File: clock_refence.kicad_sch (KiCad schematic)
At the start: 52 parts, among them J204 REFOUT_AUX_P, J205 REFOUT_AUX_N, J206 RFShield_TwoPieces, J207 REFOUT, J209 DNP, T202 TC2-1T+, U201 Si53301, U202 XC6204B33

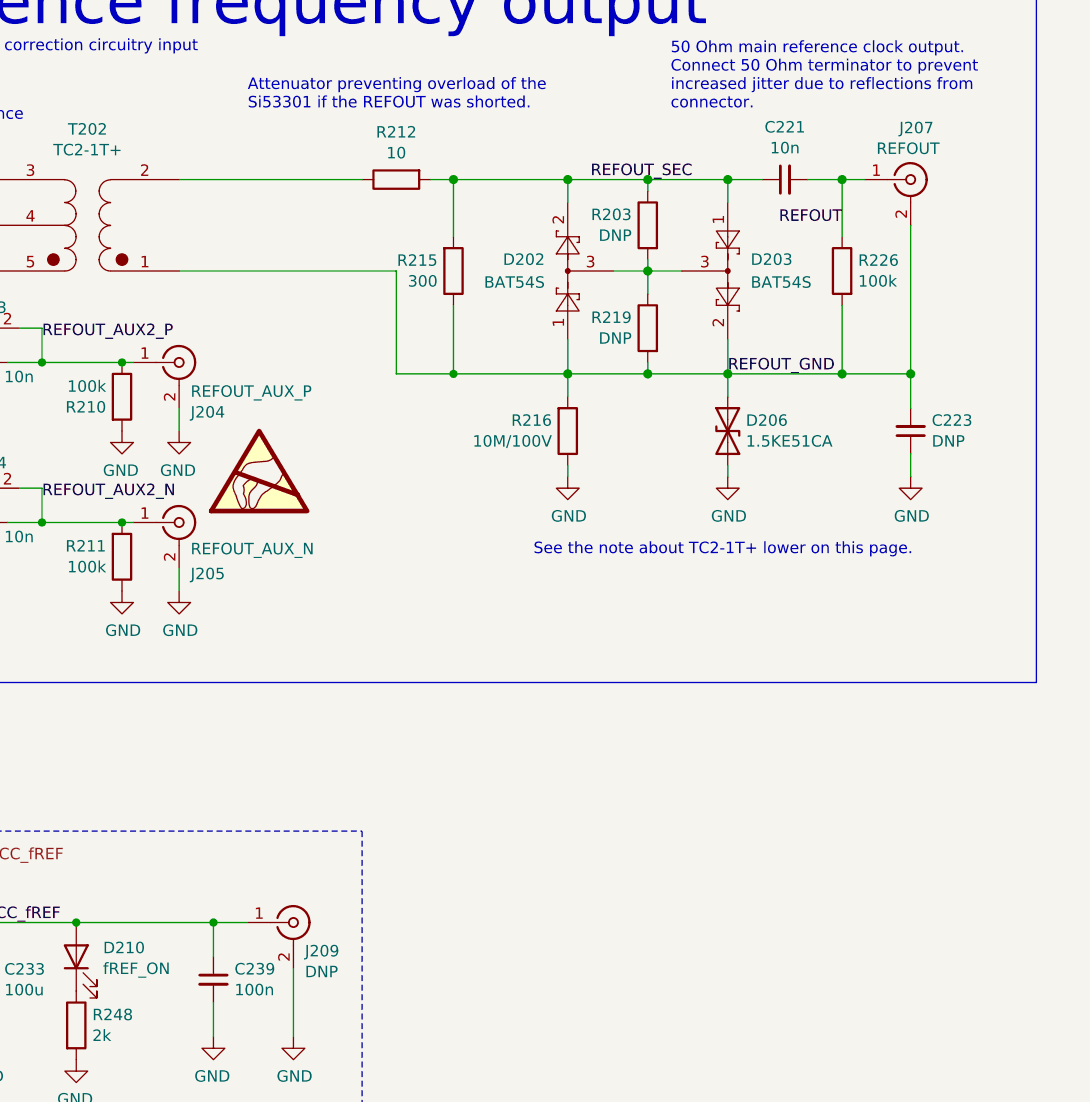
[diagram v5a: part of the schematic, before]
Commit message: Schematic fixes
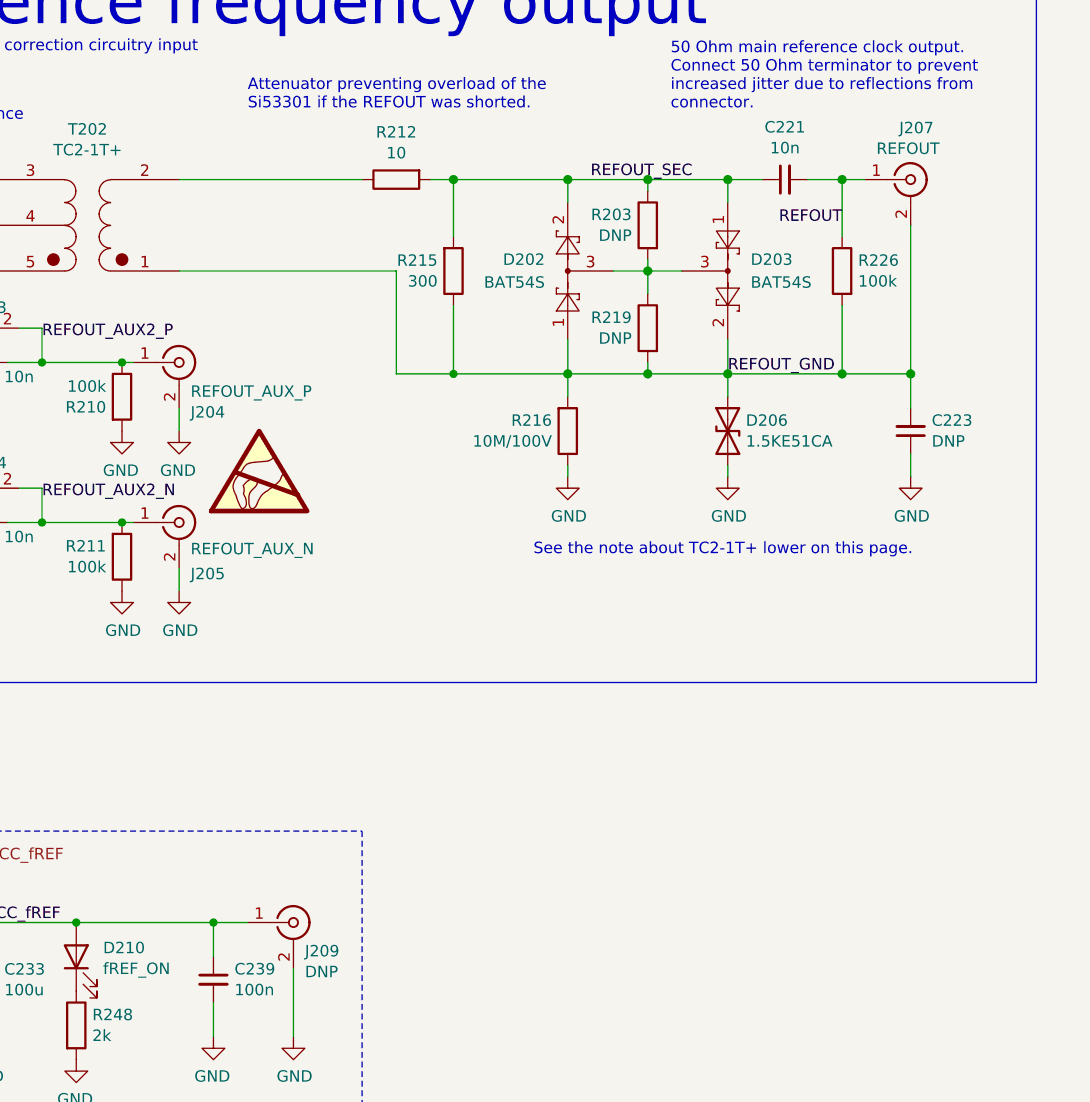
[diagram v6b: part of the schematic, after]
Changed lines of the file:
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@@
     (comment 3 "Dual channel symmetric outputs")
   )
+  (junction (at 111.76 175.26) (diameter 1.016) (color 0 0 0 0))
   (junction (at 29.21 175.26) (diameter 1.016) (color 0 0 0 0))
-  (junction (at 69.85 50.8) (diameter 1.016) (color 0 0 0 0))
+  (junction (at 118.11 130.81) (diameter 0.9144) (color 0 0 0 0))
+  (junction (at 127 130.81) (diameter 0.9144) (color 0 0 0 0))
+  (junction (at 55.88 50.8) (diameter 0.9144) (color 0 0 0 0))
+  (junction (at 127 113.03) (diameter 0.9144) (color 0 0 0 0))
+  (junction (at 207.01 92.71) (diameter 1.016) (color 0 0 0 0))
+  (junction (at 77.47 58.42) (diameter 0.9144) (color 0 0 0 0))
   (junction (at 85.09 50.8) (diameter 1.016) (color 0 0 0 0))
-  (junction (at 137.16 175.26) (diameter 0.9144) (color 0 0 0 0))
-  (junction (at 63.5 179.07) (diameter 1.016) (color 0 0 0 0))
+  (junction (at 185.42 102.87) (diameter 1.016) (color 0 0 0 0))
   (junction (at 64.77 50.8) (diameter 1.016) (color 0 0 0 0))
   (junction (at 185.42 92.71) (diameter 1.016) (color 0 0 0 0))
+  (junction (at 185.42 114.3) (diameter 1.016) (color 0 0 0 0))
+  (junction (at 163.83 114.3) (diameter 0.9144) (color 0 0 0 0))
+  (junction (at 109.22 50.8) (diameter 1.016) (color 0 0 0 0))
+  (junction (at 102.87 175.26) (diameter 1.016) (color 0 0 0 0))
+  (junction (at 105.41 113.03) (diameter 0.9144) (color 0 0 0 0))
+  (junction (at 121.92 175.26) (diameter 0.9144) (color 0 0 0 0))
+  (junction (at 176.53 114.3) (diameter 1.016) (color 0 0 0 0))
+  (junction (at 118.11 113.03) (diameter 0.9144) (color 0 0 0 0))
+  (junction (at 99.06 50.8) (diameter 0.9144) (color 0 0 0 0))
+  (junction (at 105.41 127) (diameter 0.9144) (color 0 0 0 0))
+  (junction (at 69.85 50.8) (diameter 1.016) (color 0 0 0 0))
+  (junction (at 214.63 114.3) (diameter 1.016) (color 0 0 0 0))
+  (junction (at 50.8 179.07) (diameter 0.9144) (color 0 0 0 0))
+  (junction (at 194.31 92.71) (diameter 1.016) (color 0 0 0 0))
+  (junction (at 38.1 175.26) (diameter 0.9144) (color 0 0 0 0))
+  (junction (at 176.53 92.71) (diameter 1.016) (color 0 0 0 0))
+  (junction (at 93.98 175.26) (diameter 1.016) (color 0 0 0 0))
+  (junction (at 90.17 50.8) (diameter 1.016) (color 0 0 0 0))
+  (junction (at 163.83 92.71) (diameter 1.016) (color 0 0 0 0))
   (junction (at 194.31 114.3) (diameter 1.016) (color 0 0 0 0))
-  (junction (at 194.31 92.71) (diameter 1.016) (color 0 0 0 0))
-  (junction (at 163.83 92.71) (diameter 1.016) (color 0 0 0 0))
-  (junction (at 99.06 50.8) (diameter 0.9144) (color 0 0 0 0))
-  (junction (at 121.92 175.26) (diameter 0.9144) (color 0 0 0 0))
-  (junction (at 111.76 175.26) (diameter 1.016) (color 0 0 0 0))
-  (junction (at 90.17 50.8) (diameter 1.016) (color 0 0 0 0))
-  (junction (at 118.11 113.03) (diameter 0.9144) (color 0 0 0 0))
-  (junction (at 176.53 114.3) (diameter 1.016) (color 0 0 0 0))
-  (junction (at 105.41 113.03) (diameter 0.9144) (color 0 0 0 0))
-  (junction (at 185.42 114.3) (diameter 1.016) (color 0 0 0 0))
   (junction (at 207.01 114.3) (diameter 1.016) (color 0 0 0 0))
-  (junction (at 109.22 50.8) (diameter 1.016) (color 0 0 0 0))
-  (junction (at 185.42 102.87) (diameter 1.016) (color 0 0 0 0))
-  (junction (at 163.83 114.3) (diameter 0.9144) (color 0 0 0 0))
-  (junction (at 118.11 130.81) (diameter 0.9144) (color 0 0 0 0))
-  (junction (at 102.87 175.26) (diameter 1.016) (color 0 0 0 0))
-  (junction (at 77.47 58.42) (diameter 0.9144) (color 0 0 0 0))
-  (junction (at 207.01 92.71) (diameter 1.016) (color 0 0 0 0))
-  (junction (at 214.63 114.3) (diameter 1.016) (color 0 0 0 0))
+  (junction (at 63.5 179.07) (diameter 1.016) (color 0 0 0 0))
+  (junction (at 137.16 175.26) (diameter 0.9144) (color 0 0 0 0))
   (junction (at 20.32 175.26) (diameter 1.016) (color 0 0 0 0))
-  (junction (at 93.98 175.26) (diameter 1.016) (color 0 0 0 0))
-  (junction (at 50.8 179.07) (diameter 0.9144) (color 0 0 0 0))
-  (junction (at 127 130.81) (diameter 0.9144) (color 0 0 0 0))
-  (junction (at 127 113.03) (diameter 0.9144) (color 0 0 0 0))
-  (junction (at 55.88 50.8) (diameter 0.9144) (color 0 0 0 0))
-  (junction (at 176.53 92.71) (diameter 1.016) (color 0 0 0 0))
-  (junction (at 38.1 175.26) (diameter 0.9144) (color 0 0 0 0))
-  (junction (at 105.41 127) (diameter 0.9144) (color 0 0 0 0))
   (no_connect (at 90.17 109.22))
   (no_connect (at 90.17 106.68))
@@
     (stroke (width 0) (type solid) (color 0 0 0 0))
   )
+  (wire (pts (xy 90.17 115.57) (xy 105.41 115.57))
+    (stroke (width 0) (type solid) (color 0 0 0 0))
+  )
   (wire (pts (xy 105.41 127) (xy 105.41 130.81))
     (stroke (width 0) (type solid) (color 0 0 0 0))
@@
     (stroke (width 0) (type solid) (color 0 0 0 0))
   )
-  (wire (pts (xy 90.17 115.57) (xy 105.41 115.57))
-    (stroke (width 0) (type solid) (color 0 0 0 0))
-  )
   (wire (pts (xy 38.1 175.26) (xy 66.04 175.26))
     (stroke (width 0) (type solid) (color 0 0 0 0))
@@
     (stroke (width 0) (type solid) (color 0 0 0 0))
   )
+  (wire (pts (xy 133.35 102.87) (xy 157.48 102.87))
+    (stroke (width 0) (type solid) (color 0 0 0 0))
+  )
   (wire (pts (xy 157.48 114.3) (xy 163.83 114.3))
     (stroke (width 0) (type solid) (color 0 0 0 0))
   )
-  (wire (pts (xy 133.35 102.87) (xy 157.48 102.87))
-    (stroke (width 0) (type solid) (color 0 0 0 0))
-  )
   (wire (pts (xy 185.42 113.03) (xy 185.42 114.3))
     (stroke (width 0) (type solid) (color 0 0 0 0))
@@
     (stroke (width 0) (type solid) (color 0 0 0 0))
   )
+  (polyline (pts (xy 55.88 76.2) (xy 53.34 76.2))
+    (stroke (width 0) (type default) (color 0 0 0 0))
+  )
   (polyline (pts (xy 53.34 76.2) (xy 53.34 78.74))
     (stroke (width 0) (type default) (color 0 0 0 0))
   )
-  (polyline (pts (xy 55.88 76.2) (xy 53.34 76.2))
-    (stroke (width 0) (type default) (color 0 0 0 0))
-  )
   (polyline (pts (xy 53.34 78.74) (xy 55.88 78.74))
     (stroke (width 0) (type default) (color 0 0 0 0))
@@
     (stroke (width 0) (type solid) (color 0 0 0 0))
   )
+  (wire (pts (xy 50.8 179.07) (xy 50.8 180.34))
+    (stroke (width 0) (type solid) (color 0 0 0 0))
+  )
   (wire (pts (xy 53.34 179.07) (xy 50.8 179.07))
     (stroke (width 0) (type solid) (color 0 0 0 0))
   )
-  (wire (pts (xy 50.8 179.07) (xy 50.8 180.34))
-    (stroke (width 0) (type solid) (color 0 0 0 0))
-  )
   (wire (pts (xy 194.31 110.49) (xy 194.31 114.3))
     (stroke (width 0) (type solid) (color 0 0 0 0))
@@
     (stroke (width 0) (type solid) (color 0 0 0 0))
   )
+  (polyline (pts (xy 100.33 86.36) (xy 102.87 86.36))
+    (stroke (width 0) (type default) (color 0 0 0 0))
+  )
   (polyline (pts (xy 100.33 83.82) (xy 102.87 83.82))
     (stroke (width 0) (type default) (color 0 0 0 0))
   )
-  (polyline (pts (xy 100.33 86.36) (xy 102.87 86.36))
-    (stroke (width 0) (type default) (color 0 0 0 0))
-  )
   (polyline (pts (xy 102.87 83.82) (xy 102.87 86.36))
     (stroke (width 0) (type default) (color 0 0 0 0))
@@
   (wire (pts (xy 214.63 114.3) (xy 214.63 97.79))
     (stroke (width 0) (type solid) (color 0 0 0 0))
+  )
+  (polyline (pts (xy 12.7 165.1) (xy 153.67 165.1))
+    (stroke (width 0) (type dash) (color 0 0 0 0))
+  )
+  (polyline (pts (xy 153.67 196.85) (xy 12.7 196.85))
+    (stroke (width 0) (type dash) (color 0 0 0 0))
+  )
+  (polyline (pts (xy 12.7 165.1) (xy 12.7 196.85))
+    (stroke (width 0) (type dash) (color 0 0 0 0))
   )
   (polyline (pts (xy 153.67 165.1) (xy 153.67 196.85))
     (stroke (width 0) (type dash) (color 0 0 0 0))
   )
-  (polyline (pts (xy 12.7 165.1) (xy 12.7 196.85))
-    (stroke (width 0) (type dash) (color 0 0 0 0))
-  )
-  (polyline (pts (xy 153.67 196.85) (xy 12.7 196.85))
-    (stroke (width 0) (type dash) (color 0 0 0 0))
-  )
-  (polyline (pts (xy 12.7 165.1) (xy 153.67 165.1))
-    (stroke (width 0) (type dash) (color 0 0 0 0))
-  )
   (wire (pts (xy 20.32 175.26) (xy 20.32 179.07))
     (stroke (width 0) (type solid) (color 0 0 0 0))
@@
     (stroke (width 0) (type solid) (color 0 0 0 0))
   )
+  (wire (pts (xy 118.11 130.81) (xy 127 130.81))
+    (stroke (width 0) (type solid) (color 0 0 0 0))
+  )
   (wire (pts (xy 114.3 130.81) (xy 118.11 130.81))
     (stroke (width 0) (type solid) (color 0 0 0 0))
   )
-  (wire (pts (xy 118.11 130.81) (xy 127 130.81))
-    (stroke (width 0) (type solid) (color 0 0 0 0))
-  )
   (wire (pts (xy 109.22 53.34) (xy 109.22 50.8))
     (stroke (width 0) (type solid) (color 0 0 0 0))
@@
     (stroke (width 0) (type default) (color 0 0 0 0))
   )
+  (polyline (pts (xy 228.6 22.86) (xy 228.6 148.59))
+    (stroke (width 0) (type default) (color 0 0 0 0))
+  )
+  (polyline (pts (xy 228.6 148.59) (xy 31.75 148.59))
+    (stroke (width 0) (type default) (color 0 0 0 0))
+  )
   (polyline (pts (xy 31.75 22.86) (xy 228.6 22.86))
     (stroke (width 0) (type default) (color 0 0 0 0))
   )
-  (polyline (pts (xy 228.6 22.86) (xy 228.6 148.59))
-    (stroke (width 0) (type default) (color 0 0 0 0))
-  )
-  (polyline (pts (xy 228.6 148.59) (xy 31.75 148.59))
-    (stroke (width 0) (type default) (color 0 0 0 0))
-  )
   (wire (pts (xy 63.5 101.6) (xy 64.77 101.6))
     (stroke (width 0) (type solid) (color 0 0 0 0))
@@
     (stroke (width 0) (type solid) (color 0 0 0 0))
   )
+  (wire (pts (xy 176.53 92.71) (xy 185.42 92.71))
+    (stroke (width 0) (type solid) (color 0 0 0 0))
+  )
   (wire (pts (xy 185.42 92.71) (xy 194.31 92.71))
     (stroke (width 0) (type solid) (color 0 0 0 0))
   )
-  (wire (pts (xy 176.53 92.71) (xy 185.42 92.71))
-    (stroke (width 0) (type solid) (color 0 0 0 0))
-  )
